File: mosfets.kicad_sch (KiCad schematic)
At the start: 0 parts

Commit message: everything I did while on vacation - initial schematic finished, footprints mostly assigned, and pcb layout started
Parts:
- added C19: 0.1uf, Capacitor_SMD:C_0402_1005Metric, symbol Device:C
- added IC6: KTS1622EUAA-TR, footprints:KTS1622EUAA-TR, symbol KTS1622EUAA-TR:KTS1622EUAA-TR
- added J2, J3, J4, J5, J6, J7: Screw_Terminal_01x02, symbol Connector:Screw_Terminal_01x02
- added Q1, Q11, Q3, Q5, Q7, Q9: IRLML6402, Package_TO_SOT_SMD:SOT-23, symbol Transistor_FET:IRLML6402
- added Q10, Q12, Q2, Q4, Q6, Q8: IRLML6244, Package_TO_SOT_SMD:SOT-23, symbol Transistor_FET:IRLML6244
- added R10, R11, R12, R13, R14, R15, R16, R17, R18, R19, R20, R21: 100, Resistor_SMD:R_0201_0603Metric, symbol Device:R
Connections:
- new net: Q8.1 (G), R17.1
- new net: Q10.1 (G), R19.1
- new net: J3.1 (Pin_1), Q3.3 (D)
- new net: J3.2 (Pin_2), Q4.3 (D)
- new net: J6.2 (Pin_2), Q10.3 (D)
- new net: J5.1 (Pin_1), Q7.3 (D)
- new net: J5.2 (Pin_2), Q8.3 (D)
- new net: Q7.1 (G), R16.1
- new net: J4.1 (Pin_1), Q5.3 (D)
- new net: J4.2 (Pin_2), Q6.3 (D)
- new net: Q12.1 (G), R21.1
- new net: J7.1 (Pin_1), Q11.3 (D)
- new net: J7.2 (Pin_2), Q12.3 (D)
- new net: Q3.1 (G), R12.1
- new net: Q6.1 (G), R15.1
- new net: Q1.1 (G), R11.1
- new net: J2.1 (Pin_1), Q1.3 (D)
- new net: Q9.1 (G), R18.1
- new net: C19.2, IC6.21 (VDD_P), IC6.23 (VDD_I2C)
- new net: Q2.1 (G), R10.1
- new net: J2.2 (Pin_2), Q2.3 (D)
- new net: J6.1 (Pin_1), Q9.3 (D)
- new net: Q4.1 (G), R13.1
- new net: Q5.1 (G), R14.1
- new net: Q11.1 (G), R20.1
- new net +BATT: Q1.2 (S), Q11.2 (S), Q3.2 (S), Q5.2 (S), Q7.2 (S), Q9.2 (S)
- new net GND: C19.1, IC6.18 (ADDR), IC6.25 (MC), IC6.9 (VSS), Q10.2 (S), Q12.2 (S), Q2.2 (S), Q4.2 (S), Q6.2 (S), Q8.2 (S)
- new net RST: IC6.24 (~{RESET})
- new net c1_arm: IC6.1 (P0_0), R10.2
- new net c1_fire: IC6.10 (P1_0), R11.2
- new net c2_arm: IC6.2 (P0_1), R13.2
- new net c2_fire: IC6.11 (P1_1), R12.2
- new net c3_arm: IC6.3 (P0_2), R15.2
- new net c3_fire: IC6.12 (P1_2), R14.2
- new net c4_arm: IC6.4 (P0_3), R17.2
- new net c4_fire: IC6.15 (P1_5), R16.2
- new net c5_arm: IC6.5 (P0_4), R19.2
- new net c5_fire: IC6.14 (P1_4), R18.2
- new net c6_arm: IC6.6 (P0_5), R21.2
- new net c6_fire: IC6.13 (P1_3), R20.2
- new net i2c1_sck: IC6.19 (SCL)
- new net i2c1_sda: IC6.20 (SDA)
- no-connect marks 0 -> 5

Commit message: pcb coming along, schematic way more done - I now have a lot more respect for hardware people than I did earlier
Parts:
- added D2: D, Diode_SMD:D_0402_1005Metric, symbol Device:D
- added R25: 100, Resistor_SMD:R_0805_2012Metric, symbol Device:R
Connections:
- net c2_test: now reaches J3.1 (Pin_1), Q3.3 (D)
- net at J3.2 (Pin_2), Q4.3 (D): now also J2.2 (Pin_2), J4.2 (Pin_2), J5.2 (Pin_2), J6.2 (Pin_2), J7.2 (Pin_2), Q10.3 (D), Q12.3 (D), Q2.3 (D), Q6.3 (D), Q8.3 (D), R25.1
- net c4_test: now reaches J5.1 (Pin_1), Q7.3 (D)
- net c3_test: now reaches J4.1 (Pin_1), Q5.3 (D)
- net c6_test: now reaches J7.1 (Pin_1), Q11.3 (D)
- net c1_test: now reaches J2.1 (Pin_1), Q1.3 (D)
- net c5_test: now reaches J6.1 (Pin_1), Q9.3 (D)
- new net: D2.1 (K), R25.2
- new net cont_test: D2.2 (A)
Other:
- moved on the sheet: C19, IC6, J2, J3, J4, J5, J6, J7, Q1, Q10, Q11, Q12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

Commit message: tons of work, see journal for details
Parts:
- removed J7: Screw_Terminal_01x02, symbol Connector:Screw_Terminal_01x02
- removed Q1, Q11, Q3, Q5, Q7, Q9: IRLML6402, Package_TO_SOT_SMD:SOT-23, symbol Transistor_FET:IRLML6402
- removed Q10, Q12, Q6, Q8: IRLML6244, Package_TO_SOT_SMD:SOT-23, symbol Transistor_FET:IRLML6244
- removed R16, R17, R18, R19, R20, R21: 100, Resistor_SMD:R_0201_0603Metric, symbol Device:R
- removed R25: 100, Resistor_SMD:R_0805_2012Metric, symbol Device:R
- added D1: D, Diode_SMD:D_0402_1005Metric, symbol Device:D
- added D3: D, symbol Device:D
- added IC7: IRFR9014PBF, TO228P990X238-3N, symbol IRFR9014PBF:IRFR9014PBF
- added J1: Screw_Terminal_01x02, symbol Connector:Screw_Terminal_01x02
- added Q1, Q13, Q3, Q5: IRLML6244, Package_TO_SOT_SMD:SOT-23, symbol Transistor_FET:IRLML6244
- added R26: 10k, symbol Device:R
- added R6: 100, Resistor_SMD:R_0201_0603Metric, symbol Device:R
- added R7: 100, Resistor_SMD:R_0805_2012Metric, symbol Device:R
- D2: footprint Diode_SMD:D_0402_1005Metric -> (none)
- R15: footprint Resistor_SMD:R_0201_0603Metric -> (none)
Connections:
- net c1_test is gone; now on net +12C: J2.1 (Pin_1)
- net c2_test is gone; now on net +12C: J3.1 (Pin_1)
- net c3_test is gone; now on net +12C: J4.1 (Pin_1)
- net c4_test is gone; now on net +12C: J5.1 (Pin_1)
- net c5_test is gone; now on net +12C: J6.1 (Pin_1)
- net GND: now also Q1.2 (S), Q13.2 (S), Q3.2 (S), Q5.2 (S)
- net c1_fire: now also R6.2; no longer R11.2
- net c2_fire: now also R10.2; no longer R12.2
- net c3_fire: now also R11.2; no longer R14.2
- net c4_fire: now also R12.2
- net c5_fire: now also R13.2
- net c6_fire: now also R14.2
- net cont_test: now also IC6.8 (P0_7), D1.2 (A); no longer D2.2 (A)
- net cont_test_out: now reaches J2.2 (Pin_2), J3.2 (Pin_2), J4.2 (Pin_2), J5.2 (Pin_2), J6.2 (Pin_2), Q2.3 (D), Q4.3 (D)
- net cont_test_out: now also J1.2 (Pin_2), Q1.3 (D), Q13.3 (D), Q3.3 (D), Q5.3 (D), R7.1
- net at D2.1 (K): now also R15.2
- net at R12.1: now also Q3.1 (G)
- net +12C: now reaches R15.1
- net +12C: now also IC7.4 (D), J1.1 (Pin_1)
- net at R11.1: now also Q2.1 (G)
- net at R10.1: now also Q1.1 (G); no longer Q2.1 (G)
- net at IC6.7 (P0_6): now also D2.2 (A)
- net at R14.1: now also Q5.1 (G)
- net RST renamed mos_rst
- net c1_arm renamed arm
- net arm: now also D3.2 (A); no longer R10.2
- net c2_arm: no longer names the net of IC6.2 (P0_1)
- net c2_arm: no longer R13.2
- net c3_arm: no longer names the net of IC6.3 (P0_2)
- net c3_arm: no longer R15.2
- net c4_arm: no longer names the net of IC6.4 (P0_3)
- net c5_arm: no longer names the net of IC6.5 (P0_4)
- net c6_arm: no longer names the net of IC6.6 (P0_5)
- new net: D3.1 (K), IC7.1 (G), R26.1
- new net: Q13.1 (G), R6.1
- new net: D1.1 (K), R7.2
- new net +12V: IC7.3 (S), R26.2
- no-connect marks 5 -> 1

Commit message: tons of progress on schematic and pcb - see journal for details
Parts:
- removed C19: 0.1uf, Capacitor_SMD:C_0402_1005Metric, symbol Device:C
- removed IC6: KTS1622EUAA-TR, footprints:KTS1622EUAA-TR, symbol KTS1622EUAA-TR:KTS1622EUAA-TR
- D1: footprint Diode_SMD:D_0402_1005Metric -> Diode_SMD:D_0603_1608Metric
- D2: renamed from D3; footprint (none) -> Diode_SMD:D_0603_1608Metric
- D3: renamed from D2; footprint (none) -> Diode_SMD:D_0603_1608Metric
- IC2: renamed from IC7; footprint TO228P990X238-3N -> footprints:TO228P990X238-3N
- R14: renamed from R7; value 100 -> 1k
- R15: renamed from R26; footprint (none) -> Resistor_SMD:R_0603_1608Metric
- R16: renamed from R6; footprint Resistor_SMD:R_0201_0603Metric -> Resistor_SMD:R_0603_1608Metric
- R17: renamed from R15; footprint (none) -> Resistor_SMD:R_0603_1608Metric
- R18: renamed from R10; footprint Resistor_SMD:R_0201_0603Metric -> Resistor_SMD:R_0603_1608Metric
- R19: renamed from R11; footprint Resistor_SMD:R_0201_0603Metric -> Resistor_SMD:R_0603_1608Metric
- R20: renamed from R12; footprint Resistor_SMD:R_0201_0603Metric -> Resistor_SMD:R_0603_1608Metric
- R21: renamed from R13; footprint Resistor_SMD:R_0201_0603Metric -> Resistor_SMD:R_0603_1608Metric
- R22: renamed from R14; footprint Resistor_SMD:R_0201_0603Metric -> Resistor_SMD:R_0603_1608Metric
- renumbered J1 to J4, J2 to J5, J3 to J6, J4 to J7, J5 to J8, J6 to J9, Q13 to Q1, Q1 to Q2, Q2 to Q3, Q3 to Q4, Q4 to Q5, Q5 to Q6
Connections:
- net +12V renamed +BATT
- no-connect marks 1 -> 0
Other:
- note added: "todo: see if this makes any sense at all"
- moved on the sheet: D3, R17

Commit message: worked mainly on pcb
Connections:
- net sense pin: now reaches D3.2 (A)
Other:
- note removed: "todo: see if this makes any sense at all"
- moved on the sheet: D1, D2, D3, IC2, J4, Q1, R14, R15, R16, R17

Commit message: worked on adding mosfet stuff, last of the major signal traces routed
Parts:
- J4, J5, J6, J7, J8, J9: footprint (none) -> TerminalBlock:TerminalBlock_Xinya_XY308-2.54-2P_1x02_P2.54mm_Horizontal
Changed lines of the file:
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@@
 			)
 		)
-		(property "Footprint" ""
+		(property "Footprint" "TerminalBlock:TerminalBlock_Xinya_XY308-2.54-2P_1x02_P2.54mm_Horizontal"
 			(at 133.35 95.25 0)
 			(effects
@@
 			)
 		)
-		(property "Footprint" ""
+		(property "Footprint" "TerminalBlock:TerminalBlock_Xinya_XY308-2.54-2P_1x02_P2.54mm_Horizontal"
 			(at 165.1 38.1 0)
 			(effects
@@
 			)
 		)
-		(property "Footprint" ""
+		(property "Footprint" "TerminalBlock:TerminalBlock_Xinya_XY308-2.54-2P_1x02_P2.54mm_Horizontal"
 			(at 238.76 38.1 0)
 			(effects
@@
 			)
 		)
-		(property "Footprint" ""
+		(property "Footprint" "TerminalBlock:TerminalBlock_Xinya_XY308-2.54-2P_1x02_P2.54mm_Horizontal"
 			(at 92.71 38.1 0)
 			(effects
@@
 			)
 		)
-		(property "Footprint" ""
+		(property "Footprint" "TerminalBlock:TerminalBlock_Xinya_XY308-2.54-2P_1x02_P2.54mm_Horizontal"
 			(at 128.27 38.1 0)
 			(effects
@@
 			)
 		)
-		(property "Footprint" ""
+		(property "Footprint" "TerminalBlock:TerminalBlock_Xinya_XY308-2.54-2P_1x02_P2.54mm_Horizontal"
 			(at 201.93 38.1 0)
 			(effects

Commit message: mosfet schematic done I hope
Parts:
- removed D1, D2, D3: D, Diode_SMD:D_0603_1608Metric, symbol Device:D
- removed Q1, Q2, Q3, Q4, Q5, Q6: IRLML6244, Package_TO_SOT_SMD:SOT-23, symbol Transistor_FET:IRLML6244
- added Q1, Q2, Q3, Q4, Q5, Q8: DMN3404L, Package_TO_SOT_SMD:SOT-23, symbol Transistor_FET:DMN3404L
- added Q7: MMBT2222A, Package_TO_SOT_SMD:SOT-23, symbol Transistor_BJT:MMBT2222A
- added R29: 1k, Resistor_SMD:R_0402_1005Metric, symbol Device:R
- added R30: 100, Resistor_SMD:R_0603_1608Metric, symbol Device:R
- R14: value 1k -> 100k; footprint Resistor_SMD:R_0805_2012Metric -> Resistor_SMD:R_0603_1608Metric
- R16: value 100 -> 1k
- R17: value 100 -> 12k
- R19: value 100 -> 3k
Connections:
- net +12C: now also R14.1, R17.2; no longer R17.1
- net GND: now also R19.1, Q1.2 (S), Q2.2 (S), Q3.2 (S), Q4.2 (S), Q5.2 (S), Q7.3 (C), Q8.2 (S)
- net arm: now also R29.2
- net c3_fire: now also R20.2; no longer R19.2
- net c4_fire: now also R21.2; no longer R20.2
- net c5_fire: now also R22.2; no longer R21.2
- net c6_fire: now also R30.2; no longer R22.2
- net cont_test_out: now also R17.1, R19.2; no longer J4.2 (Pin_2), J5.2 (Pin_2), J6.2 (Pin_2), J7.2 (Pin_2), J8.2 (Pin_2), J9.2 (Pin_2), R14.1
- net at IC2.1 (G), R15.1: now also Q7.2 (E)
- net at R22.1: now also Q4.1 (G)
- net at R18.1: now also Q1.1 (G)
- net at R16.1: now also Q8.1 (G)
- net at R20.1: now also Q2.1 (G)
- net at R21.1: now also Q3.1 (G)
- net +3.3V: now reaches R14.2
- new net: J7.2 (Pin_2), Q3.3 (D)
- new net: J4.2 (Pin_2), Q8.3 (D)
- new net: Q7.1 (B), R29.1
- new net: J8.2 (Pin_2), Q4.3 (D)
- new net: J5.2 (Pin_2), Q1.3 (D)
- new net: J9.2 (Pin_2), Q5.3 (D)
- new net: Q5.1 (G), R30.1
- new net: J6.2 (Pin_2), Q2.3 (D)
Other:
- moved on the sheet: IC2, J4, J5, R15, R16, R18

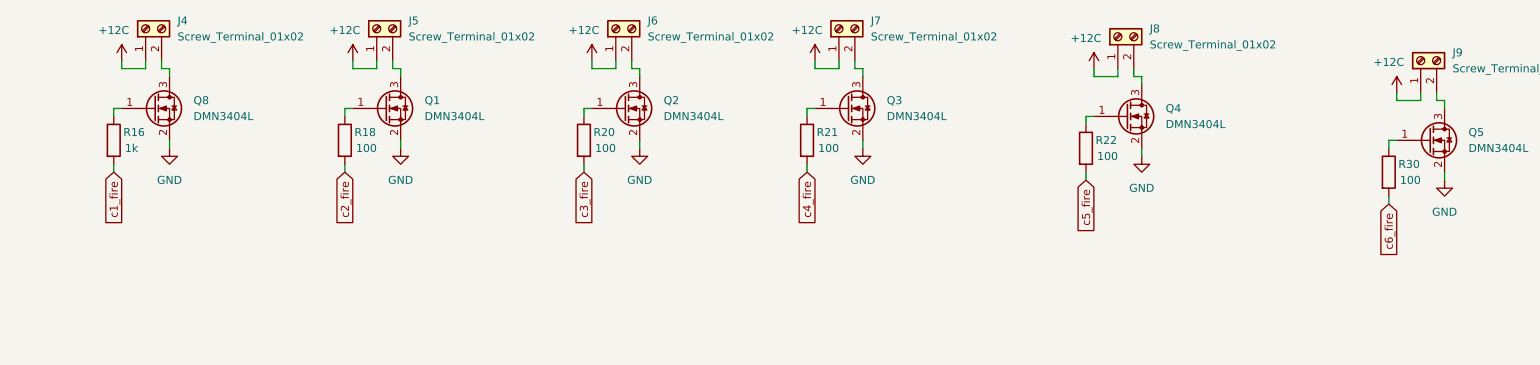
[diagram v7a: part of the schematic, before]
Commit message: mosfet schematic should be finalized
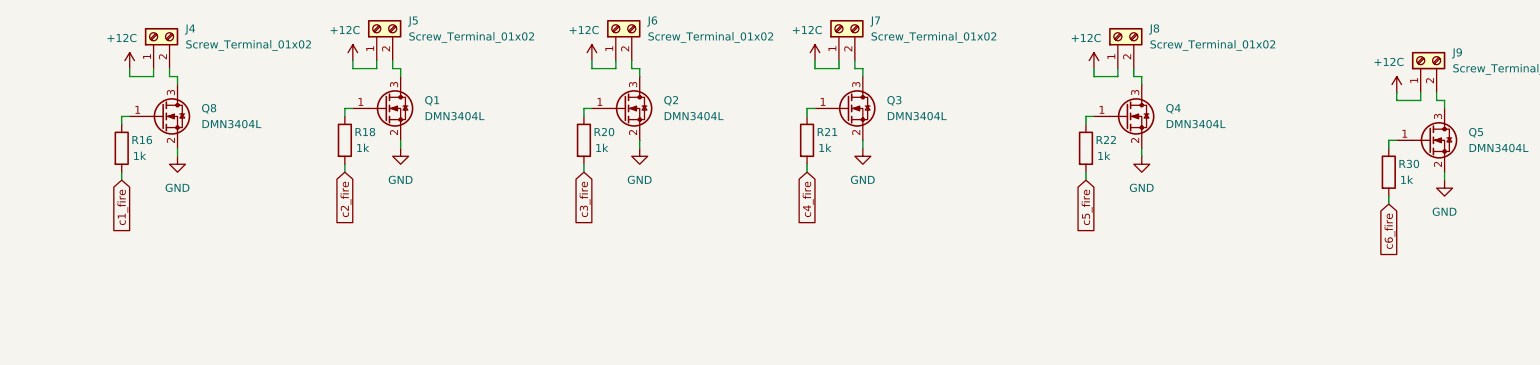
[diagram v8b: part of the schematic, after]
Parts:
- R18, R20, R21, R22, R30: value 100 -> 1k
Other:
- moved on the sheet: J4, Q8, R16
